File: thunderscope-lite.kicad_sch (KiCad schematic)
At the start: 0 parts

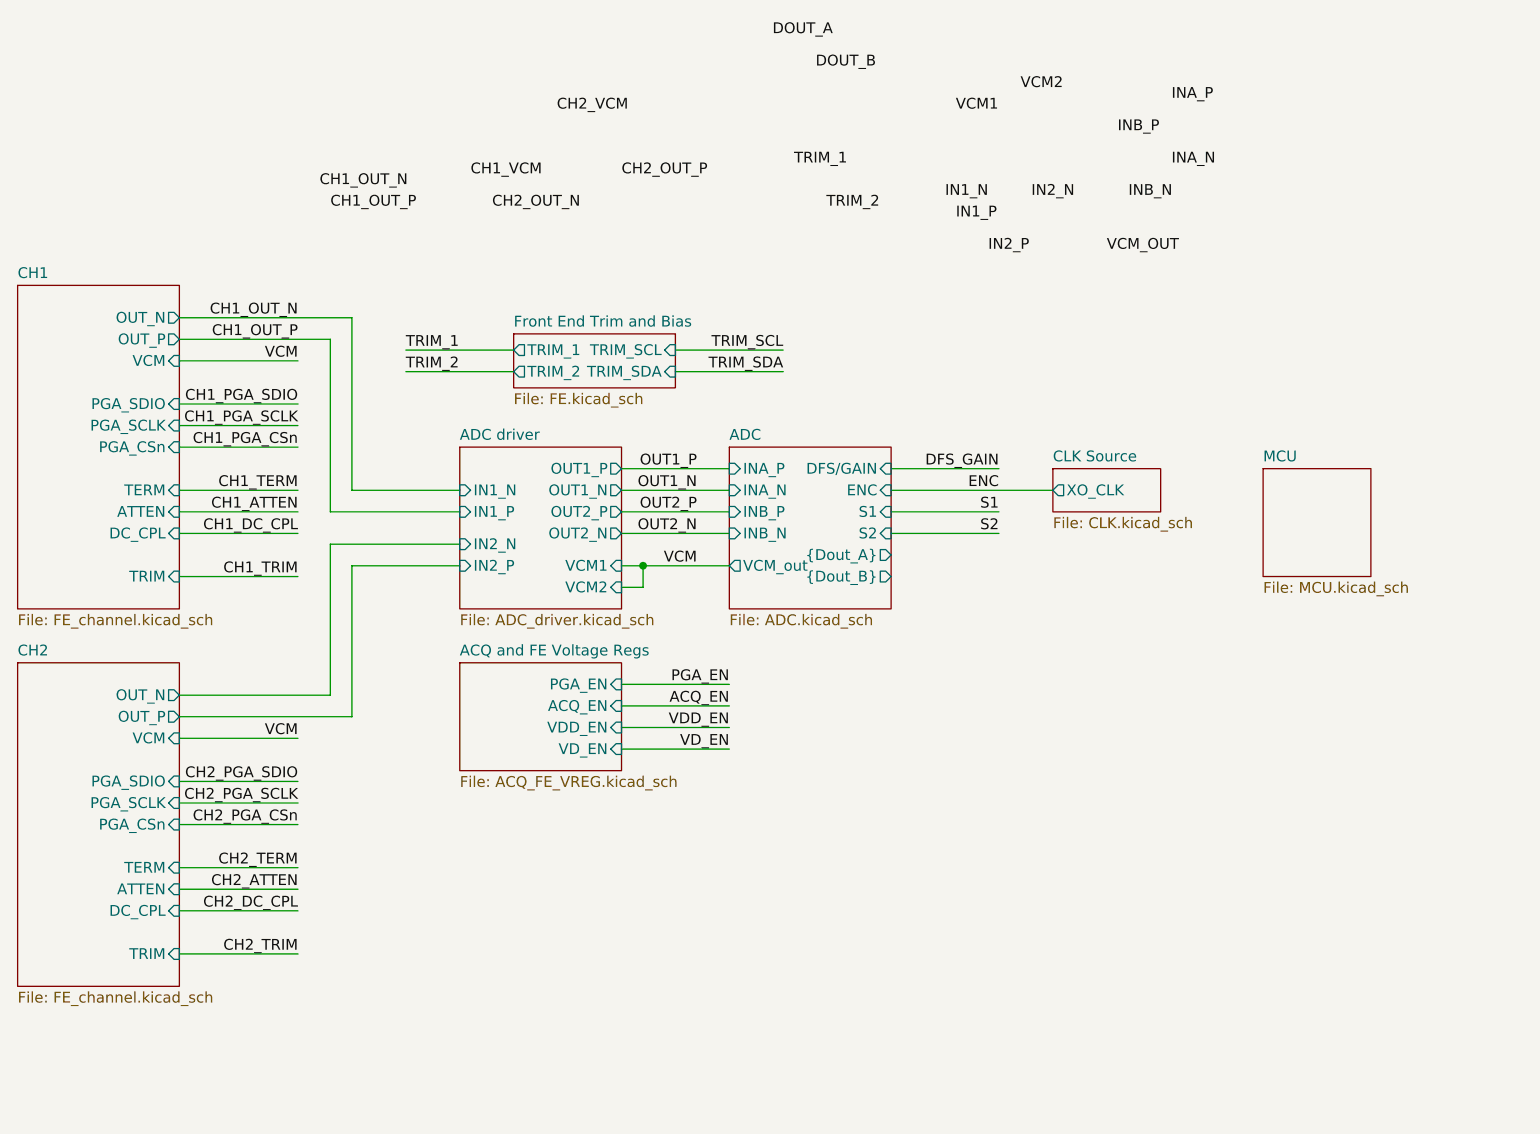
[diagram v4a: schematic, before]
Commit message: schematic complete. no ERC errors
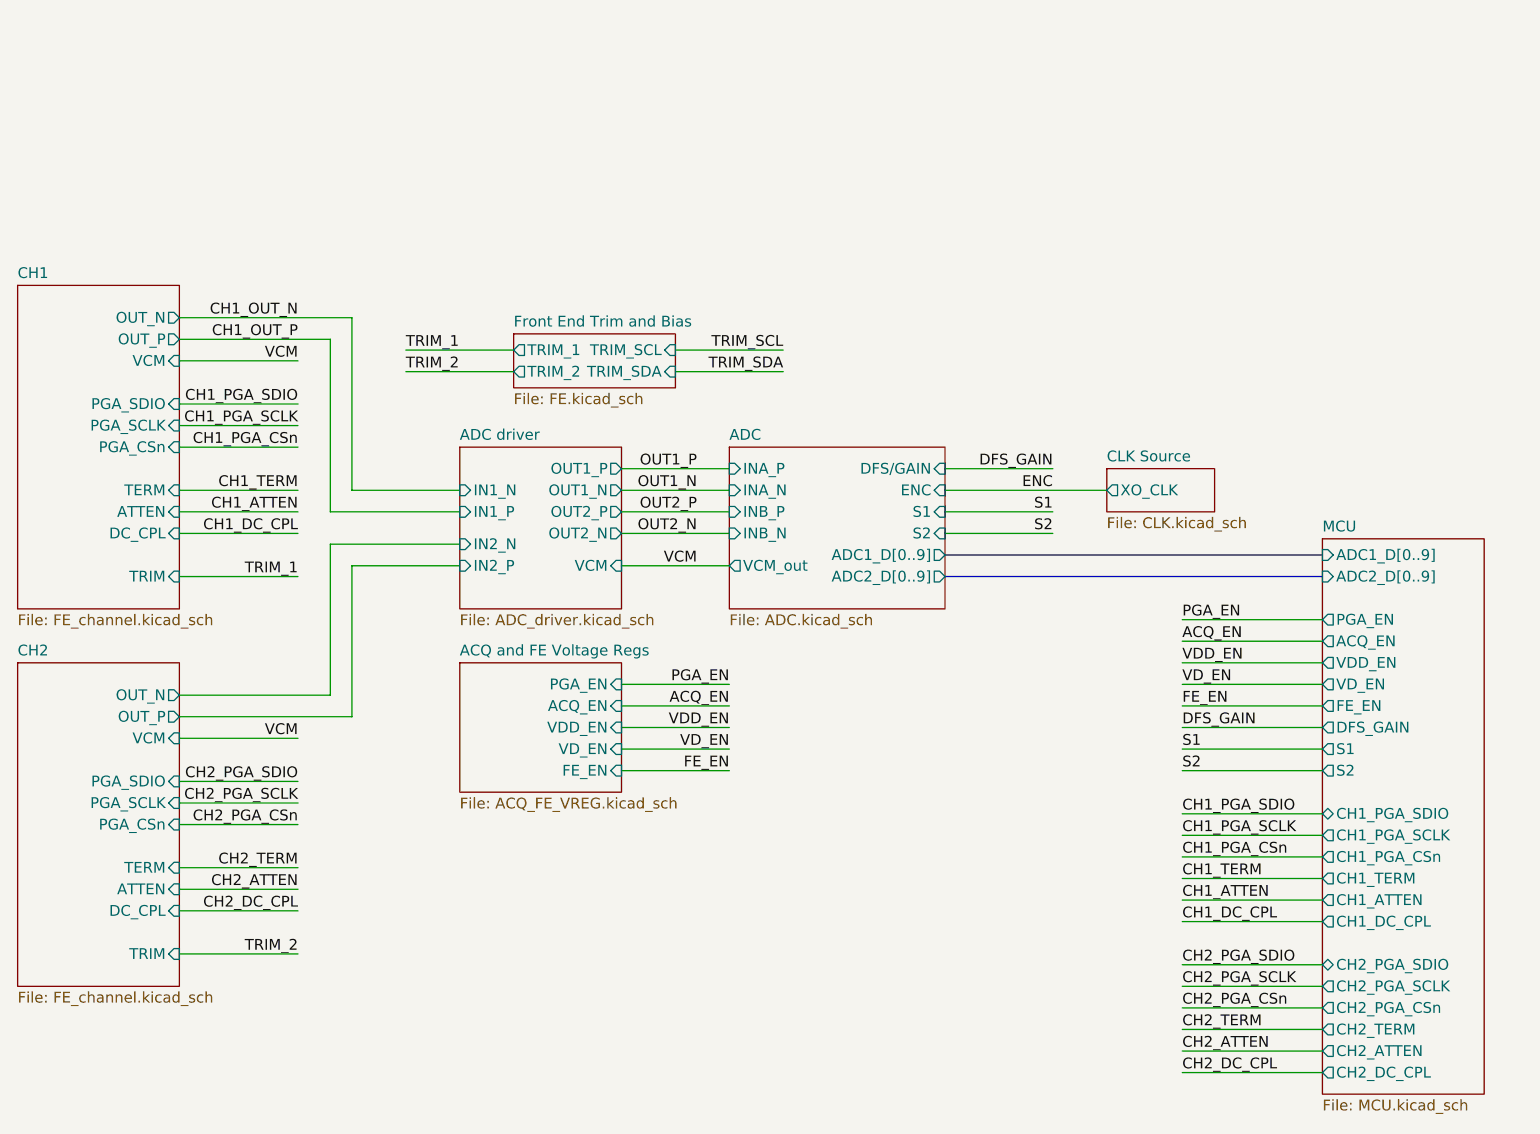
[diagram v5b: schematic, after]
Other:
- sheet ACQ and FE Voltage Regs ports: added FE_EN; removed none
- sheet ADC ports: added ADC1_D[0..9], ADC2_D[0..9]; removed {Dout_A}, {Dout_B}
- sheet ADC driver ports: added VCM; removed VCM1, VCM2
- sheet MCU ports: added ACQ_EN, ADC1_D[0..9], ADC2_D[0..9], CH1_ATTEN, CH1_DC_CPL, CH1_PGA_CSn, CH1_PGA_SCLK, CH1_PGA_SDIO, CH1_TERM, CH2_ATTEN, CH2_DC_CPL, CH2_PGA_CSn, CH2_PGA_SCLK, CH2_PGA_SDIO, CH2_TERM, DFS_GAIN, FE_EN, PGA_EN, S1, S2, VDD_EN, VD_EN; removed none
